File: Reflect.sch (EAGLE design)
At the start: 8 parts, among them IC1 QRE1113GR, IC2 QRE1113GR

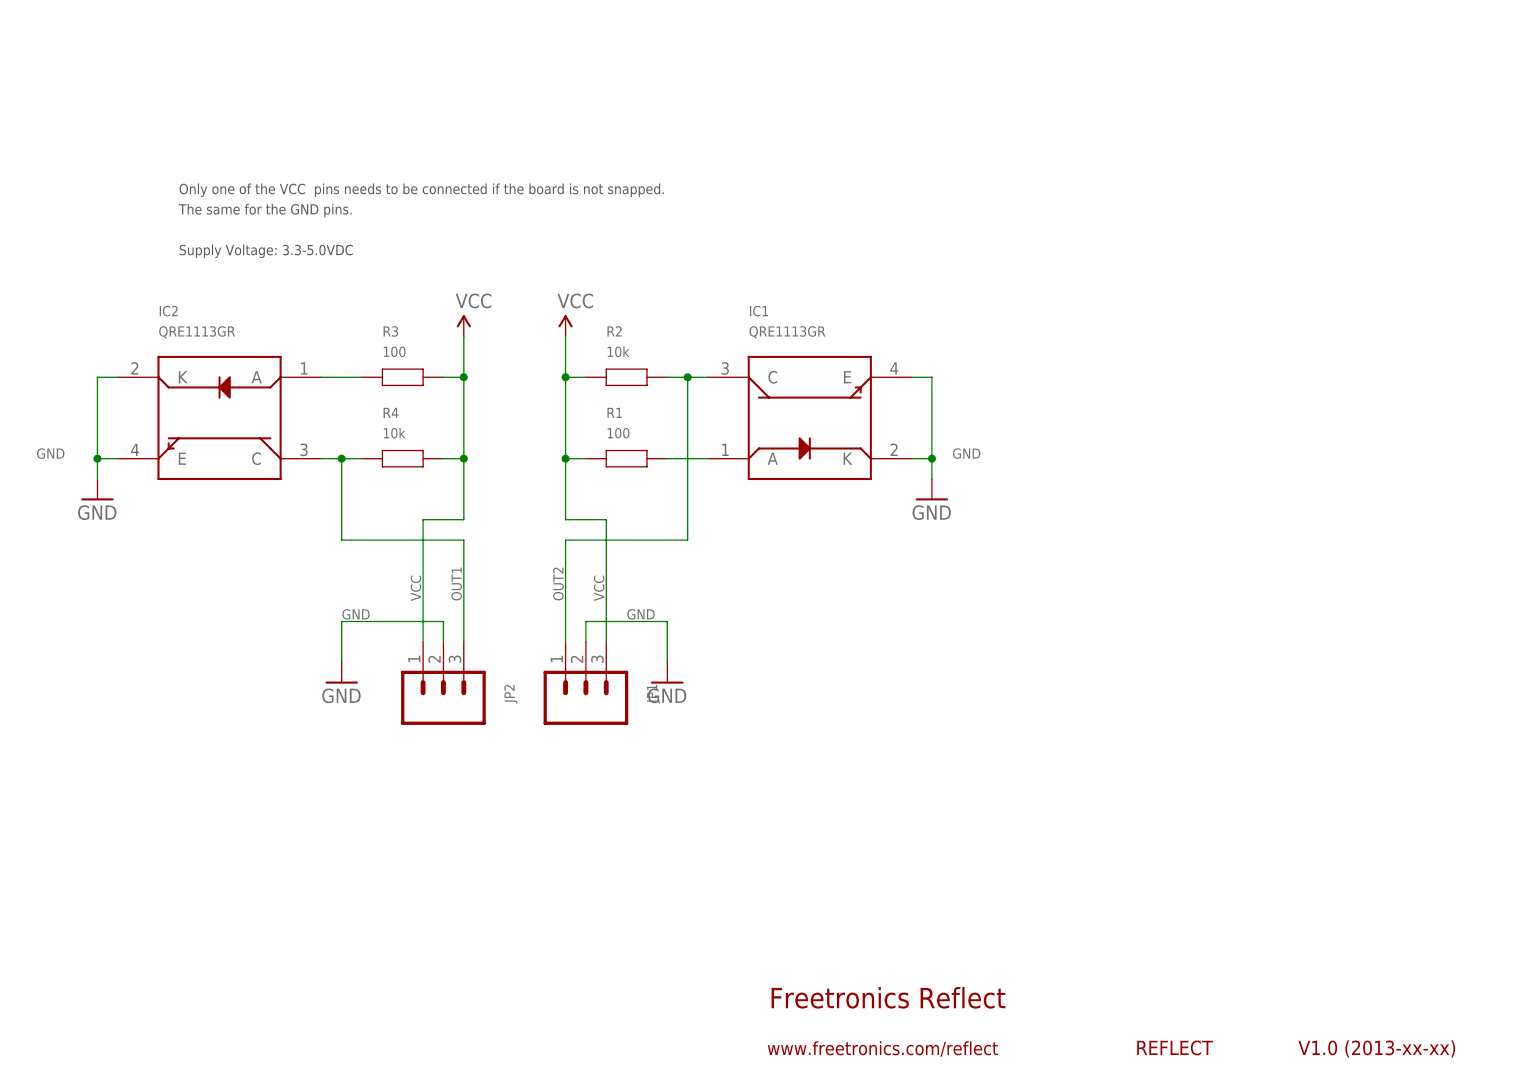
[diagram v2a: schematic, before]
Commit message: Tweaks to schematic and PCB for v1.0 release
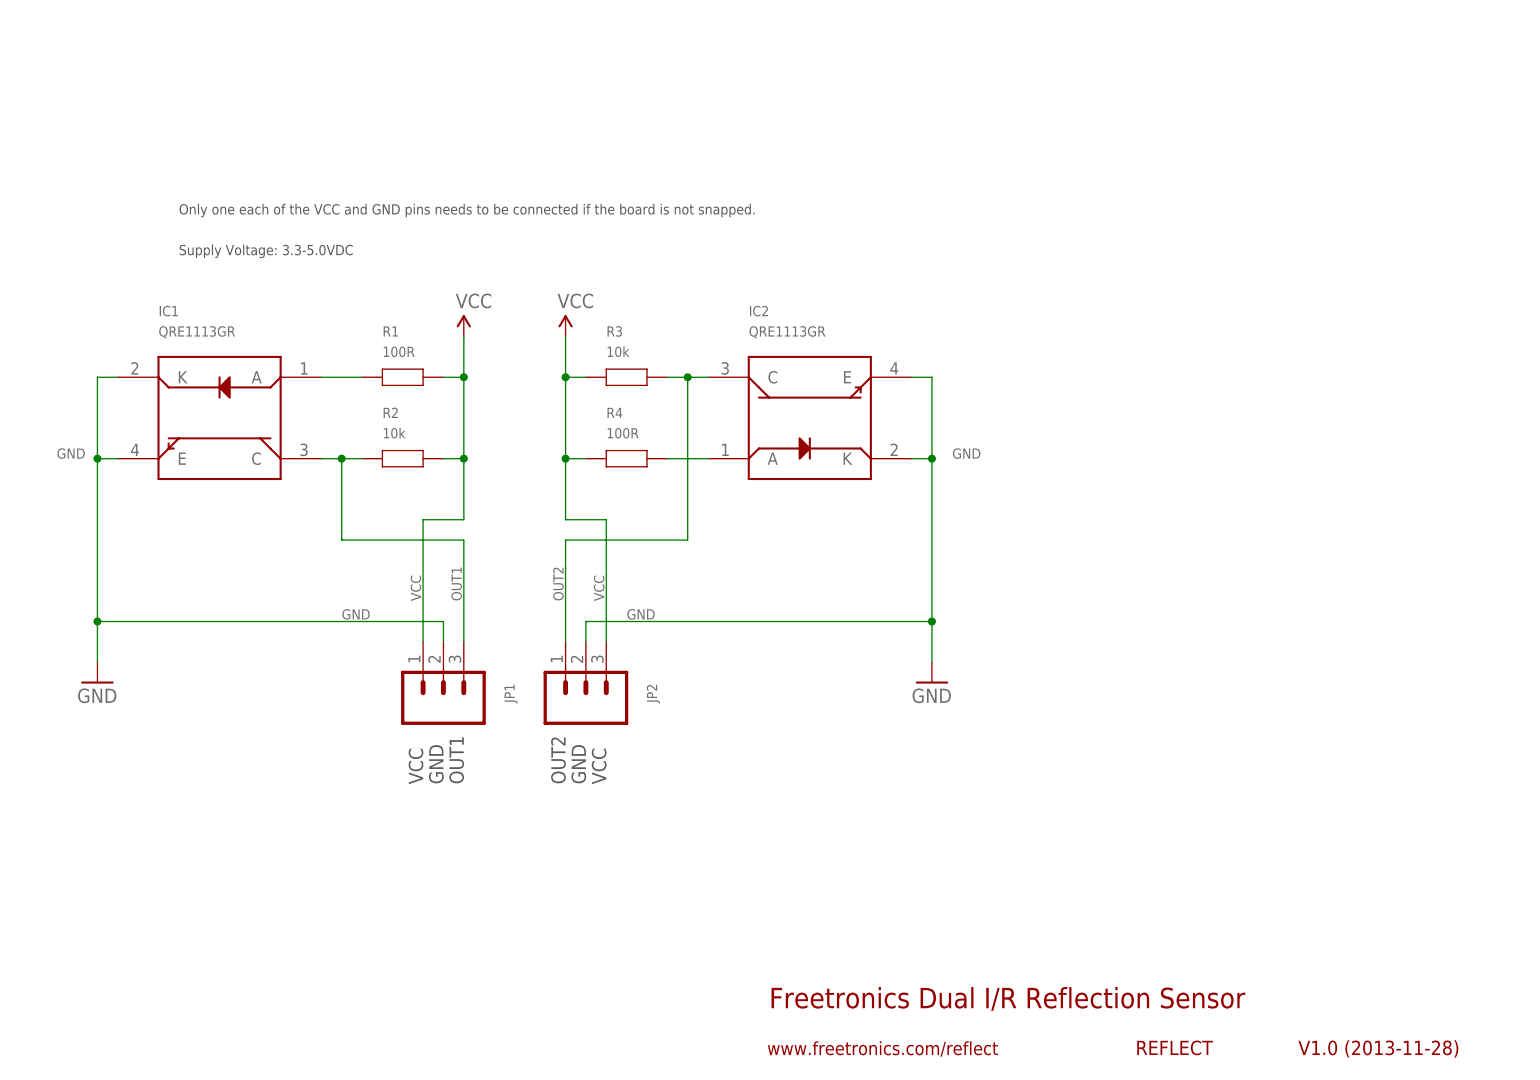
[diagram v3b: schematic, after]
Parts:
- R1: value 100 -> 100R
- R3: value 100 -> 10k
- R4: value 10k -> 100R
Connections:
- net N$1: now also IC1.A, R1.1; no longer IC2.A, R3.1
- net N$3: now also IC2.A, R4.2; no longer IC1.A, R1.2
- net OUT1: now also IC1.C, JP1.3, R2.1; no longer IC2.C, JP2.3, R4.1
- net OUT2: now also IC2.C, JP2.1, R3.2; no longer IC1.C, JP1.1, R2.2
- net VCC: now also JP1.1, JP2.3, R1.2, R2.2, R3.1, R4.1; no longer JP1.3, JP2.1, R1.1, R2.1, R3.2, R4.2
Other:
- note added: "Freetronics Dual I/R Reflection Sensor"
- note added: "GND"
- note added: "OUT1"
- note added: "OUT2"
- note added: "Only one each of the VCC and GND pins needs to be connected if the board is not snapped."
- note added: "V1.0 (2013-11-28)"
- note added: "VCC"
- note removed: "Freetronics Reflect"
- note removed: "Only one of the VCC pins needs to be connected if the board is not snapped."
- note removed: "The same for the GND pins."
- note removed: "V1.0 (2013-xx-xx)"
- moved on the sheet: IC1, IC2, JP1, JP2, R1, R2, R3, R4
